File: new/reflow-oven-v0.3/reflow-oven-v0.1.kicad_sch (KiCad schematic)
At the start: 13 parts, among them IC1 MBED-LPC1768, J1 Pot, J2 Conn_01x08_Female, J3 Conn_01x01_Female, J4 Conn_01x01_Female, J5 Conn_01x05_Female, SW1 SW_Push, U1 MOC3041M

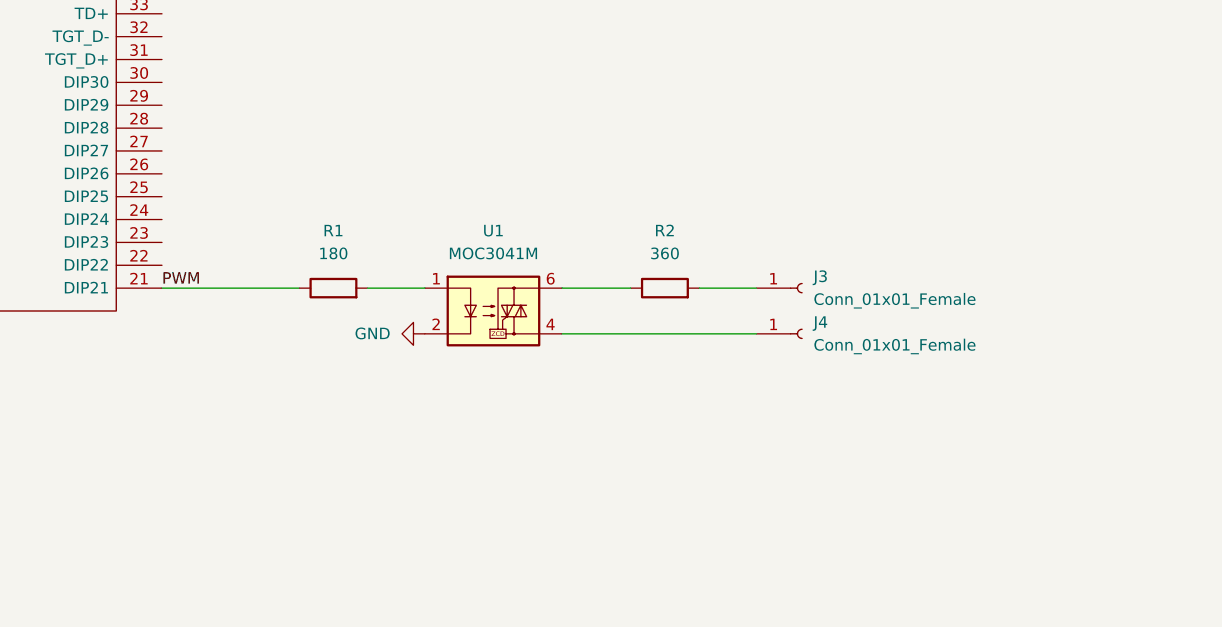
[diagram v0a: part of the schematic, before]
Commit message: Updated cad schematic *added pwm pinout extra
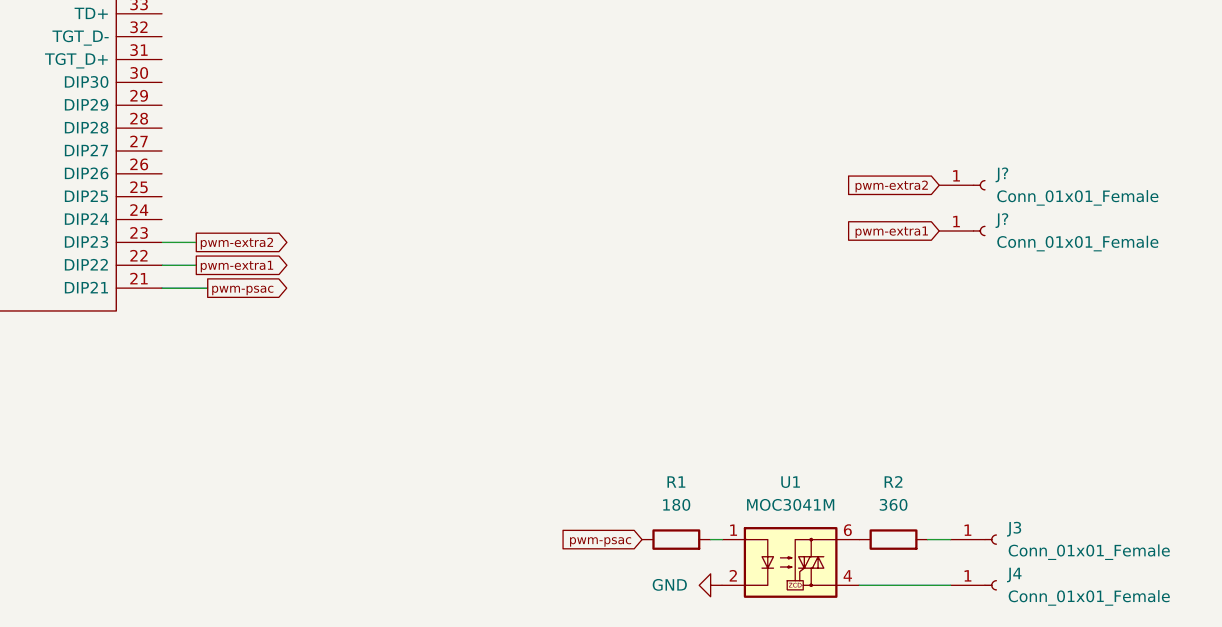
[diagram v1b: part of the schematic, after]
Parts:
- added J? (x2): Conn_01x01_Female, Connector_PinHeader_2.54mm:PinHeader_1x01_P2.54mm_Vertical, symbol Connector:Conn_01x01_Female
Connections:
- net pwm-extra1: now reaches IC1.22 (DIP22)
- net pwm-extra1: now also J?.1 (Pin_1)
- net pwm-extra2: now reaches IC1.23 (DIP23)
- net pwm-extra2: now also J?.1 (Pin_1)
- net PWM renamed pwm-psac
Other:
- moved on the sheet: J3, J4, R1, R2, U1
